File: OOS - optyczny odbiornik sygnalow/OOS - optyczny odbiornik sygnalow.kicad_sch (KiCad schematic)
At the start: 27 parts, among them J101 Conn_Coaxial, U101 OPA300AIDBVR, U102 OPA300AIDBVR

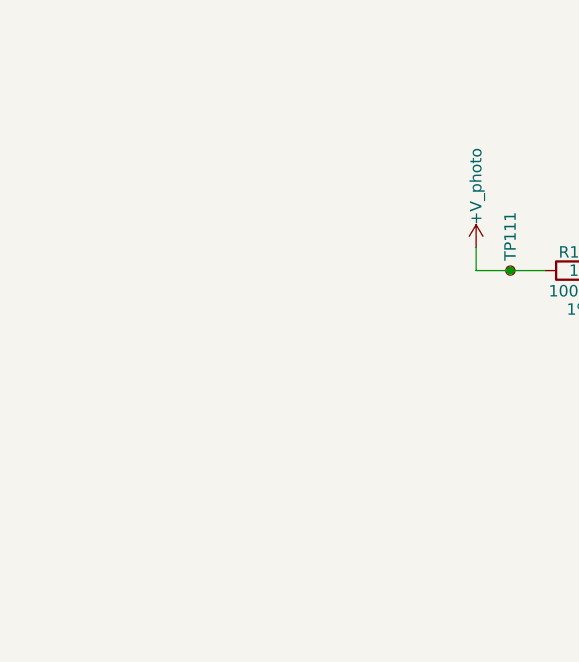
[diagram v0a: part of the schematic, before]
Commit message: Dodanie zlacz na +V_photo, +5V i 0V
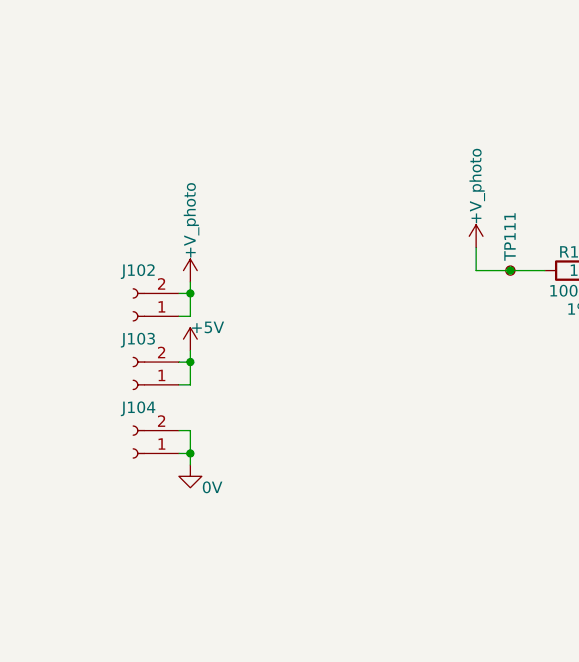
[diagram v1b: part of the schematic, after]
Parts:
- added J102, J103, J104: Conn_01x02_Socket, Connector_PinHeader_2.54mm:PinHeader_1x02_P2.54mm_Vertical, symbol Connector:Conn_01x02_Socket
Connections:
- net +5V: now also J103.1 (Pin_1), J103.2 (Pin_2)
- net +V_photo: now also J102.1 (Pin_1), J102.2 (Pin_2)
- net 0V: now also J104.1 (Pin_1), J104.2 (Pin_2)

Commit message: Dodanie zasilania i rezystora do pinu enable
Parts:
- added R109: 10k, Resistor_SMD:R_0402_1005Metric, symbol Device:R
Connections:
- net +5V: now also R109.1
- net OPA300_En: now also R109.2
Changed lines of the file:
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@@
+	(wire
+		(pts
+			(xy 106.68 127) (xy 106.68 139.7)
+		)
+		(stroke
+			(width 0)
+			(type default)
+		)
+	)
 	(wire
 		(pts
@@
 	(wire
 		(pts
+			(xy 73.66 139.7) (xy 106.68 139.7)
+		)
+		(stroke
+			(width 0)
+			(type default)
+		)
+	)
+	(wire
+		(pts
 			(xy 83.82 110.49) (xy 83.82 111.76)
 		)
@@
 		)
 	)
-	(wire
-		(pts
-			(xy 93.98 127) (xy 106.68 127)
-		)
-		(stroke
-			(width 0)
-			(type default)
-		)
-	)
 	(polyline
 		(pts
@@
 		)
 	)
+	(wire
+		(pts
+			(xy 73.66 129.54) (xy 73.66 139.7)
+		)
+		(stroke
+			(width 0)
+			(type default)
+		)
+	)
 	(polyline
 		(pts
@@
 	(wire
 		(pts
+			(xy 73.66 120.65) (xy 73.66 121.92)
+		)
+		(stroke
+			(width 0)
+			(type default)
+		)
+	)
+	(wire
+		(pts
 			(xy 83.82 100.33) (xy 83.82 101.6)
 		)
@@
 	)
 	(label "OPA300_En"
-		(at 93.98 127 0)
+		(at 76.2 139.7 0)
 		(effects
 			(font
@@
 	)
 	(symbol
+		(lib_id "Device:R")
+		(at 73.66 125.73 0)
+		(unit 1)
+		(exclude_from_sim no)
+		(in_bom yes)
+		(on_board yes)
+		(dnp no)
+		(property "Reference" "R109"
+			(at 74.93 124.46 0)
+			(effects
+				(font
+					(size 1.27 1.27)
+				)
+				(justify left)
+			)
+		)
+		(property "Value" "10k"
+			(at 74.93 127 0)
+			(effects
+				(font
+					(size 1.27 1.27)
+				)
+				(justify left)
+			)
+		)
+		(property "Footprint" "Resistor_SMD:R_0402_1005Metric"
+			(at 71.882 125.73 90)
+			(effects
+				(font
+					(size 1.27 1.27)
+				)
+				(hide yes)
+			)
+		)
+		(property "Datasheet" "https://eu.mouser.com/datasheet/2/447/PYu_RC_Group_51_RoHS_L_11-1984063.pdf"
+			(at 73.66 125.73 0)
+			(effects
+				(font
+					(size 1.27 1.27)
+				)
+				(hide yes)
+			)
+		)
+		(property "Description" "Resistor"
+			(at 73.66 125.73 0)
+			(effects
+				(font
+					(size 1.27 1.27)
+				)
+				(hide yes)
+			)
+		)
+		(property "Power Rating" "62.5 mW"
+			(at 73.66 125.73 0)
+			(effects
+				(font
+					(size 1.27 1.27)
+				)
+				(hide yes)
+			)
+		)
+		(property "Tolerance" "1 %"
+			(at 73.66 125.73 0)
+			(effects
+				(font
+					(size 1.27 1.27)
+				)
+				(hide yes)
+			)
+		)
+		(property "Temperature Coefficient" "100 PPM / C"
+			(at 73.66 125.73 0)
+			(effects
+				(font
+					(size 1.27 1.27)
+				)
+				(hide yes)
+			)
+		)
+		(property "Voltage Rating" "50V"
+			(at 73.66 125.73 0)
+			(effects
+				(font
+					(size 1.27 1.27)
+				)
+				(hide yes)
+			)
+		)
+		(property "MPN" "RC0603JR-13100KL"
+			(at 73.66 125.73 0)
+			(effects
+				(font
+					(size 1.27 1.27)
+				)
+				(hide yes)
+			)
+		)
+		(property "Voltage" ""
+			(at 73.66 125.73 0)
+			(effects
+				(font
+					(size 1.27 1.27)
+				)
+			)
+		)
+		(property "Voltge Rating" ""
+			(at 73.66 125.73 0)
+			(effects
+				(font
+					(size 1.27 1.27)
+				)
+			)
+		)
+		(pin "1"
+		)
+		(pin "2"
+		)
+		(instances
+			(project "OOS - optyczny odbiornik sygnalow"
+				(path "/635760df-3241-4f53-aa67-bcf04a8ecd85"
+					(reference "R109")
+					(unit 1)
+				)
+			)
+		)
+	)
+	(symbol
 		(lib_id "Device:C")
 		(at 106.68 81.28 90)
@@
 					(unit 1)
 				)
+			)
+		)
+	)
+	(symbol
+		(lib_id "power:+5V")
+		(at 73.66 120.65 0)
+		(unit 1)
+		(exclude_from_sim no)
+		(in_bom yes)
+		(on_board yes)
+		(dnp no)
+		(property "Reference" "#PWR0114"
+			(at 73.66 124.46 0)
+			(effects
+				(font
+					(size 1.27 1.27)
+				)
+				(hide yes)
+			)
+		)
+		(property "Value" "+5V"
+			(at 73.66 118.11 0)
+			(effects
+				(font
+					(size 1.27 1.27)
+				)
+				(justify left)
+			)
+		)
+		(property "Footprint" ""
+			(at 73.66 120.65 0)
+			(effects
+				(font
+					(size 1.27 1.27)
+				)
+				(hide yes)
+			)
+		)
+		(property "Datasheet" ""
+			(at 73.66 120.65 0)
+			(effects
+				(font
+					(size 1.27 1.27)
+				)
+				(hide yes)
+			)
+		)
+		(property "Description" "Power symbol creates a global label with name \"+5V\""
+			(at 73.66 120.65 0)
+			(effects
+				(font
+					(size 1.27 1.27)
+				)
+				(hide yes)
+			)
+		)
+		(pin "1"
+		)
+		(instances
+			(project "OOS - optyczny odbiornik sygnalow"
+				(path "/635760df-3241-4f53-aa67-bcf04a8ecd85"
+					(reference "#PWR0114")
+					(unit 1)
+				)

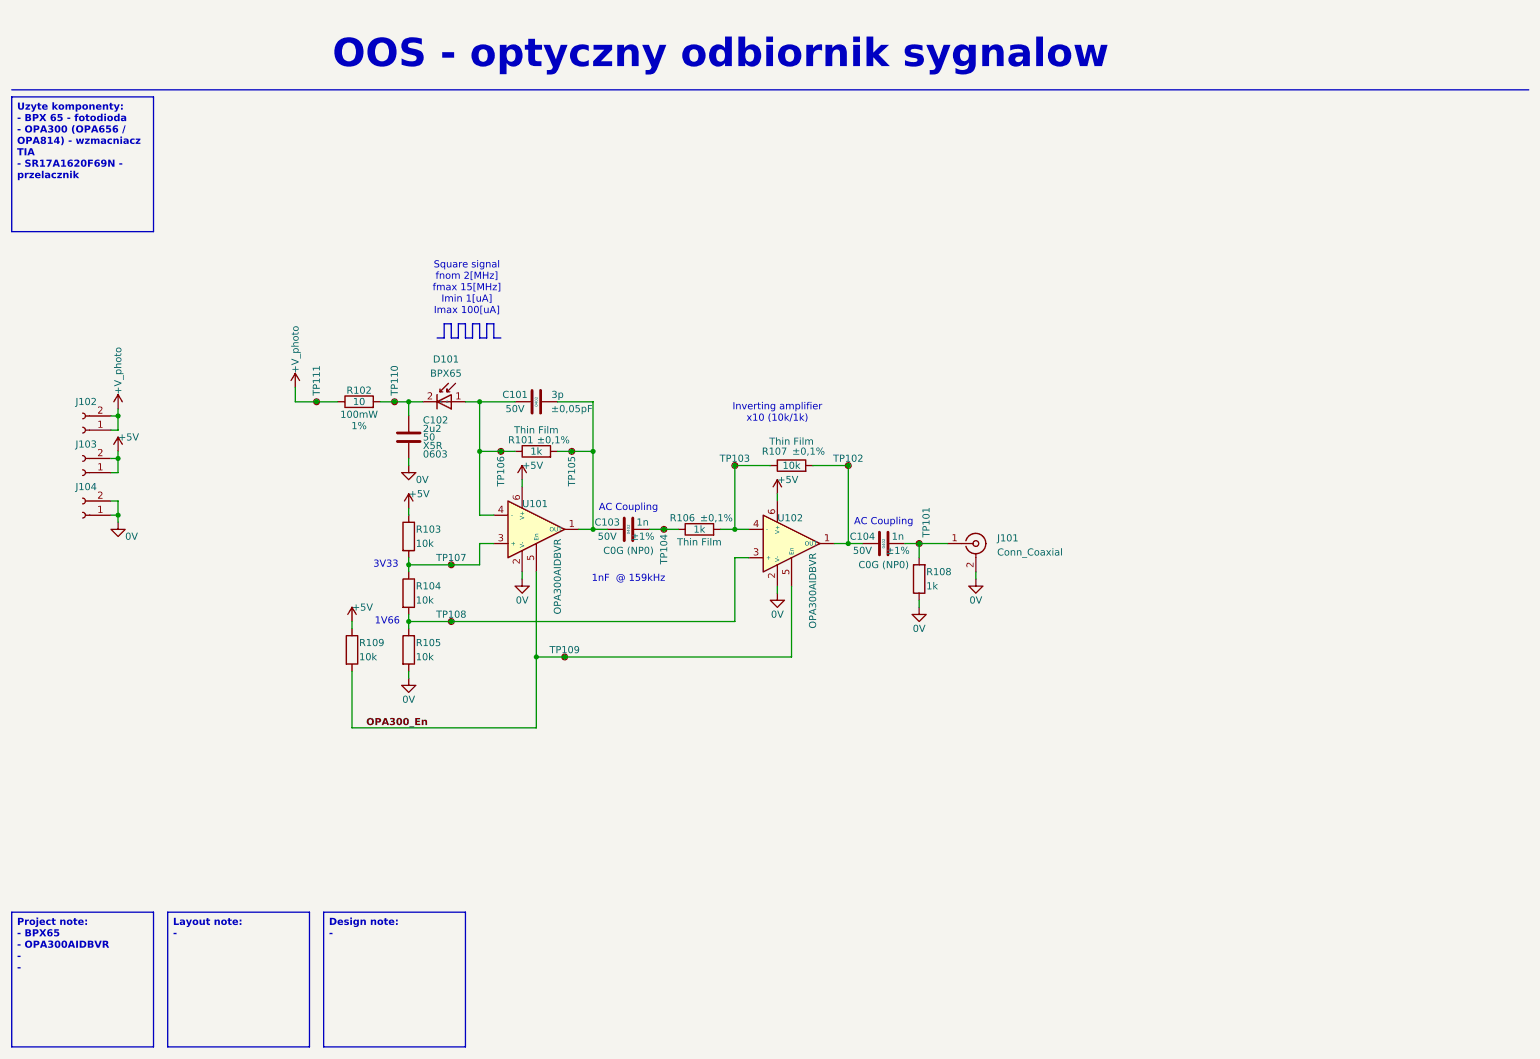
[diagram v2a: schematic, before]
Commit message: Dodane kondensatory odsprzegajace, poukladane informacje dla kazdego elementu zasilania
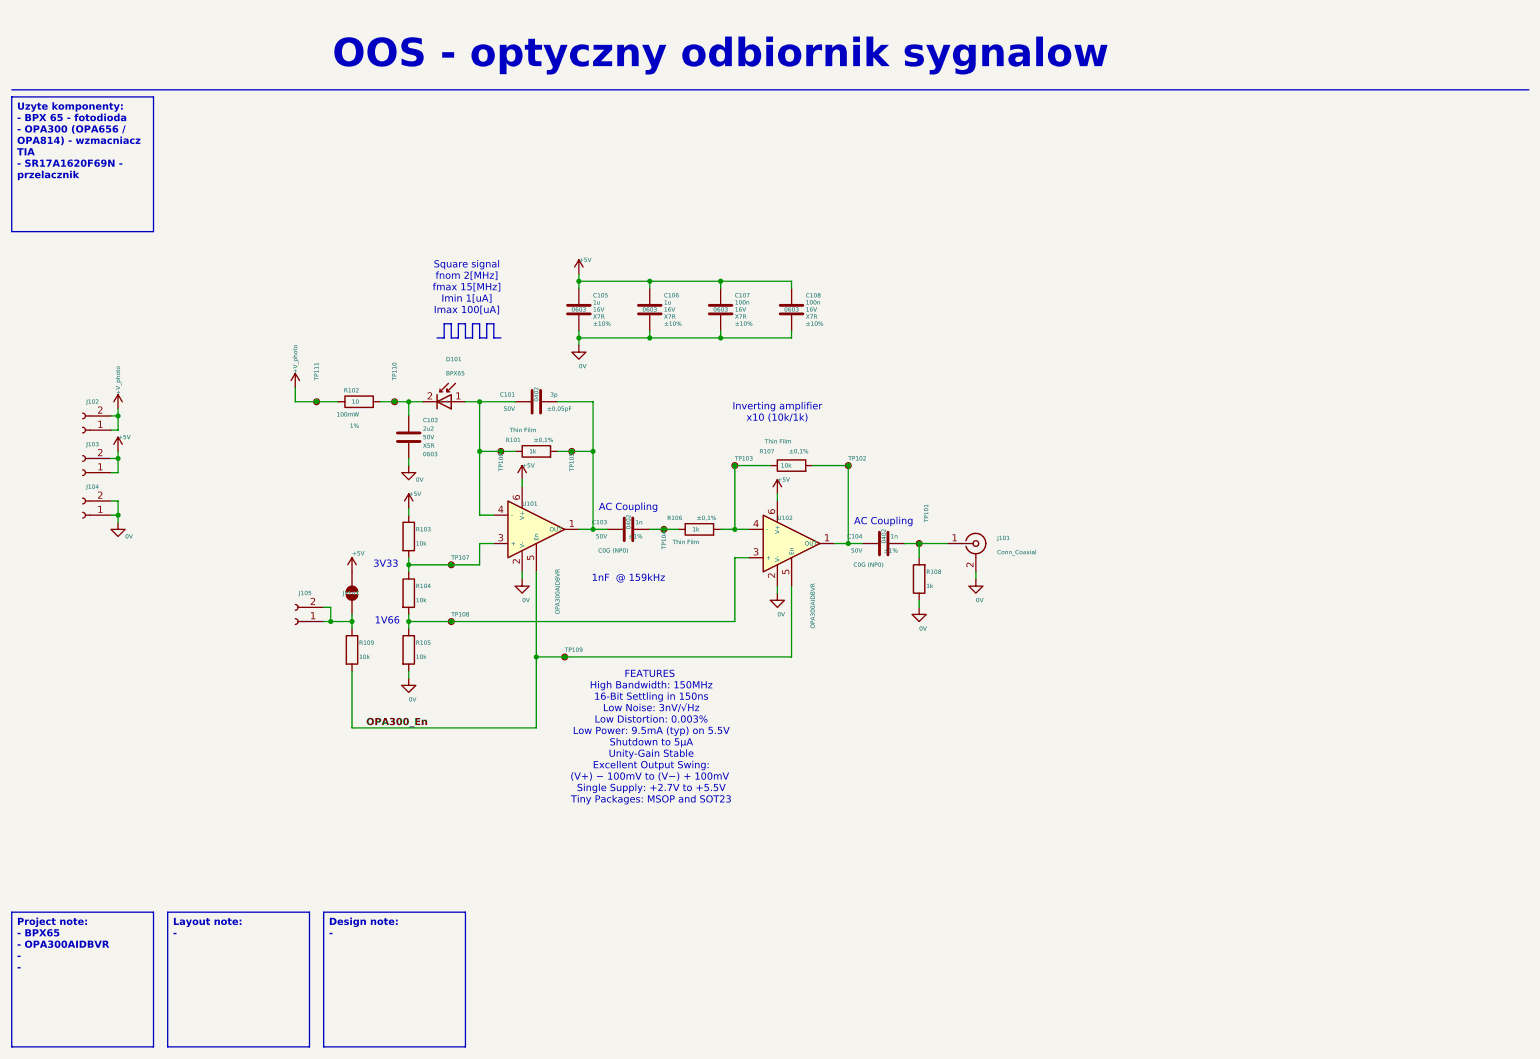
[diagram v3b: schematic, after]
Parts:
- added C105, C106: 1u, Resistor_SMD:R_0603_1608Metric, symbol Device:C
- added C107, C108: 100n, Resistor_SMD:R_0603_1608Metric, symbol Device:C
- added J105: Conn_01x02_Socket, Connector_PinHeader_2.54mm:PinHeader_1x02_P2.54mm_Vertical, symbol Connector:Conn_01x02_Socket
- added JP101: SolderJumper_2_Open, symbol Jumper:SolderJumper_2_Open
- C102: Voltage Rating 50 -> 50V
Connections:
- net +5V: now also C105.1, C106.1, C107.1, C108.1, JP101.2 (B); no longer R109.1
- net 0V: now also C105.2, C106.2, C107.2, C108.2
- new net: J105.1 (Pin_1), J105.2 (Pin_2), JP101.1 (A), R109.1
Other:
- note added: "FEATURES High Bandwidth: 150MHz 16-Bit Settling in 150ns Low Noise: 3nV/√Hz Low Distortion: 0.003% Low Power: 9.5mA (typ) on 5.5V Shutdown to 5μA Unity-Gain Stable Excellent Output Swing: (V+) − 100mV to (V−) + 100mV Single Supply: +2.7V to +5.5V Tiny Packages: MSOP and SOT23"

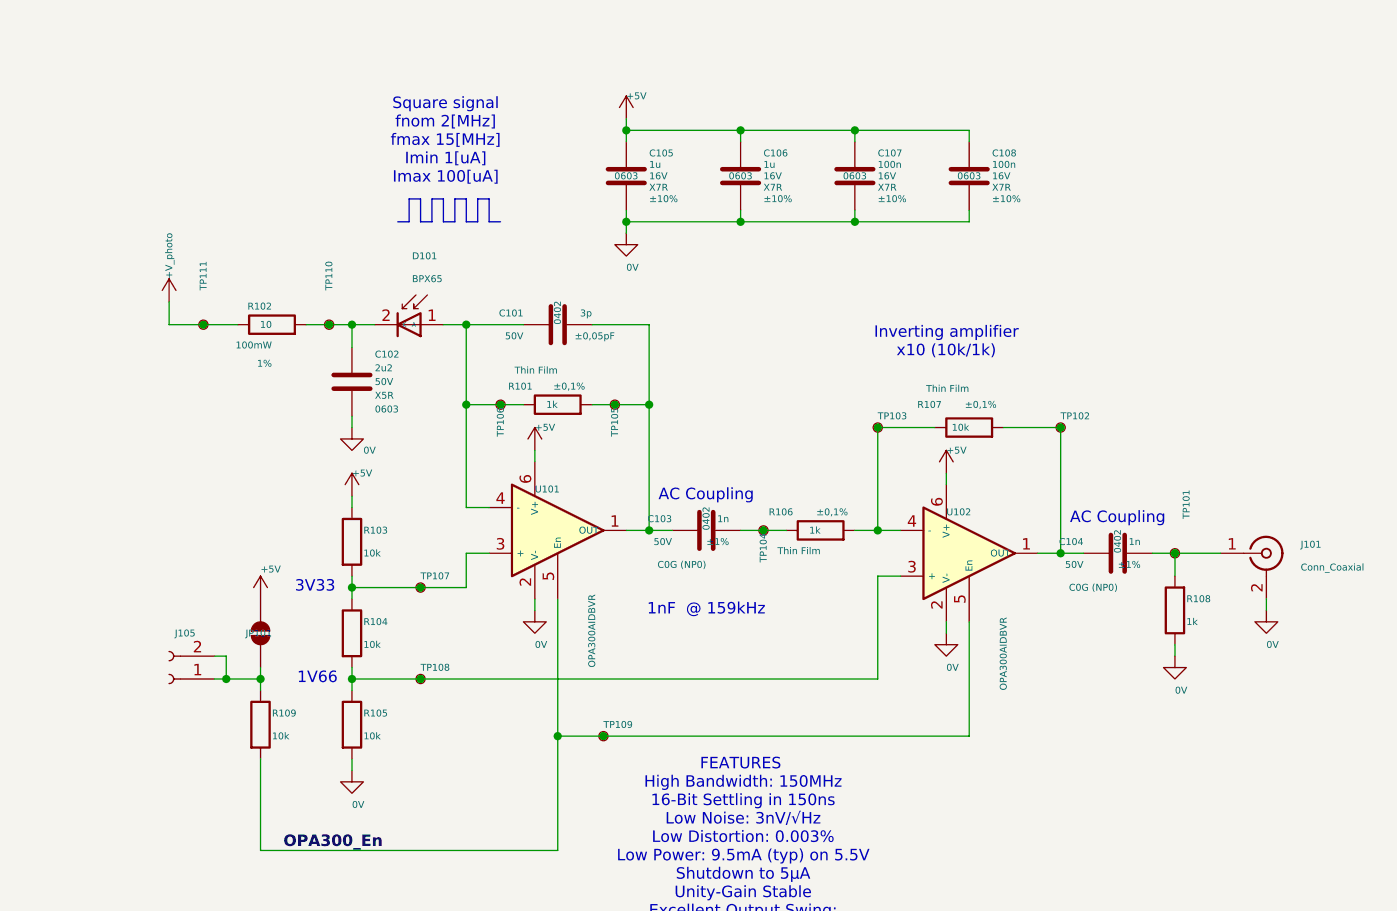
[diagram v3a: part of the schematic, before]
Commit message: Schemat po review z AI, wpisane co potrzeba zmienic
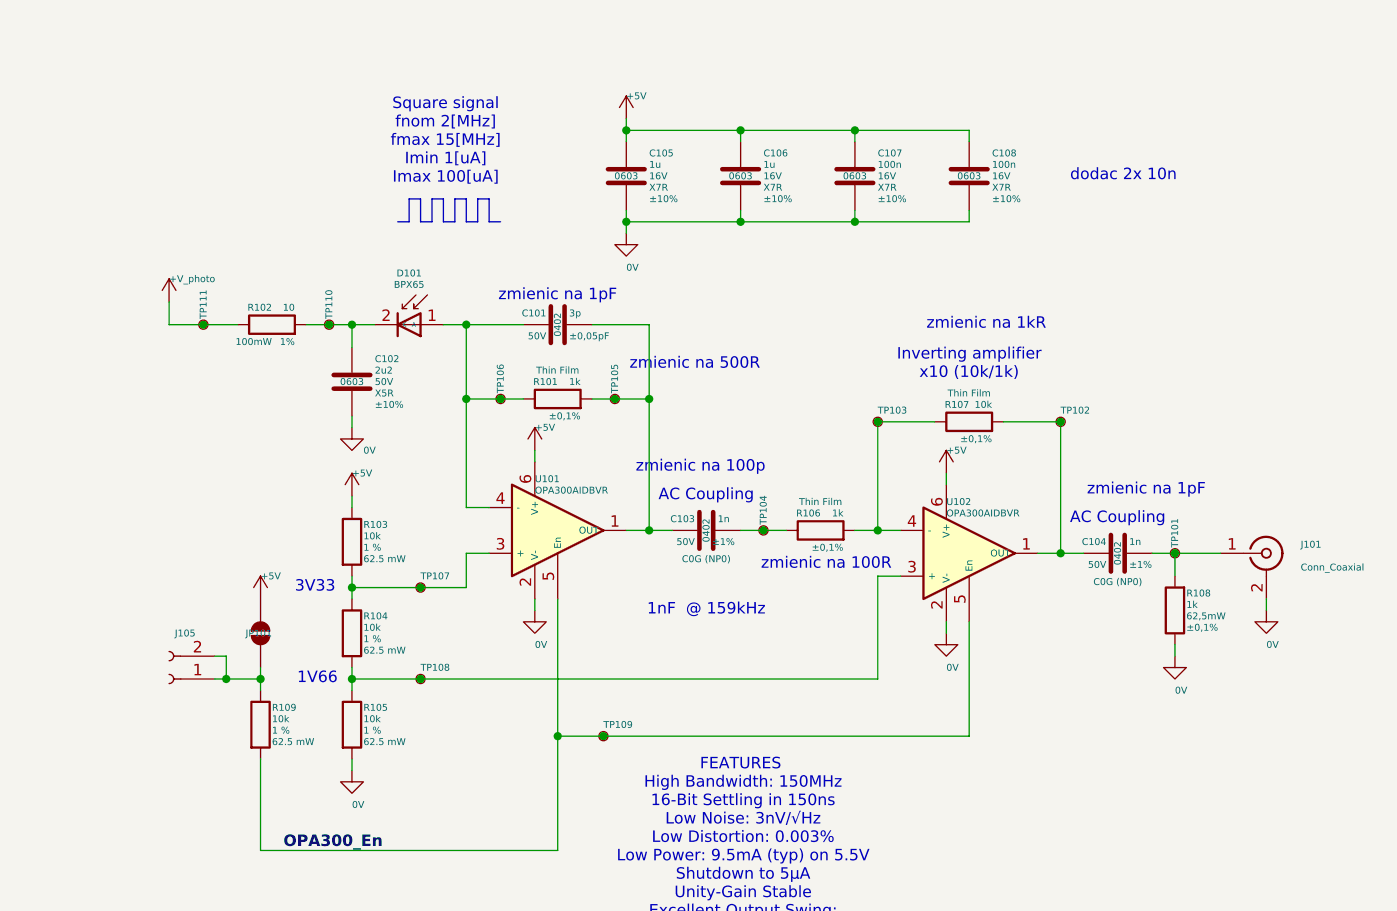
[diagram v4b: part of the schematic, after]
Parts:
- C104: Tolerance ±1% -> ±1%
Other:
- note added: "dodac 2x 10n"
- note added: "zmienic na 100R"
- note added: "zmienic na 100p"
- note added: "zmienic na 1kR"
- note added: "zmienic na 1pF"
- note added: "zmienic na 500R"
- moved on the sheet: R101, R107, TP102, TP103, TP105, TP106

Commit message: Dodanie dalszych komentarzy po przegladzie
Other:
- note added: "dodac 10n"
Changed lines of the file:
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@@
+		)
+	)
+	(text "dodac 10n"
+		(exclude_from_sim no)
+		(at 73.025 90.805 0)
+		(effects
+			(font
+				(size 1.27 1.27)
+			)
 		)
 	)
